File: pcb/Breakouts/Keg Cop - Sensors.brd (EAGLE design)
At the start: 17.8 x 53.8 mm, 6 parts

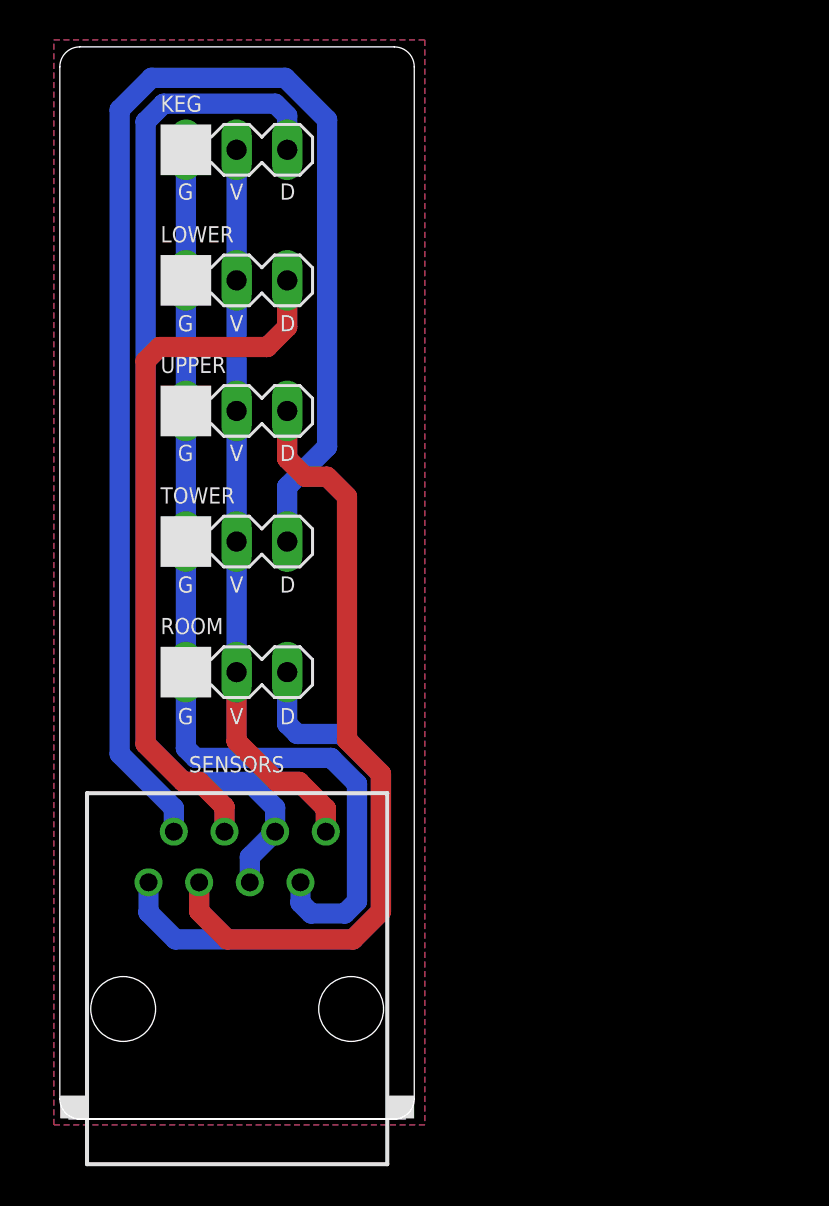
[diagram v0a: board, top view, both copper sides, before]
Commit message: Updates to names and traces
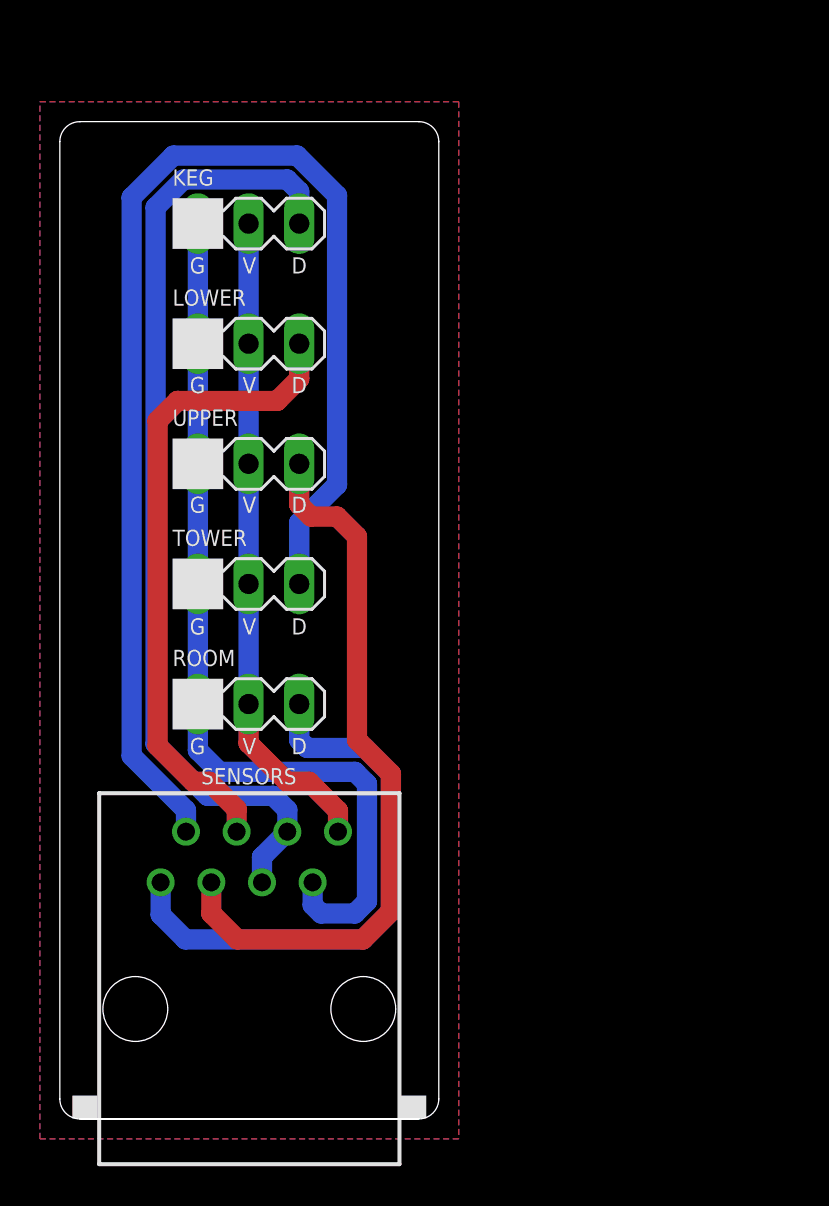
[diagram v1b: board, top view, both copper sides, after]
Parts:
- moved KEG 3.75 mm to (6.92, 44.9)
- moved LOWER 3.23 mm to (6.92, 38.9)
- moved UPPER 2.72 mm to (6.92, 32.8)
- moved TOWER 2.21 mm to (6.92, 26.8)
- moved ROOM 1.71 mm to (6.92, 20.8)
- moved SENSORS 0.61 mm to (9.50, 5.51)
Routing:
- net TDAT: track 71.2 -> 65.2 mm
- net KDAT: track 52.7 -> 48.7 mm
- net GND: track 49.6 -> 45.8 mm
- net 5V: track 36.7 -> 33.0 mm
- net LDAT: track 35.9 -> 32.4 mm
- net UDAT: track 39.4 -> 36.8 mm
- net RDAT: track 29.5 -> 28.3 mm
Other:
- board size 17.8 x 53.8 mm -> 19 x 50 mm

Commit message: New sensor board
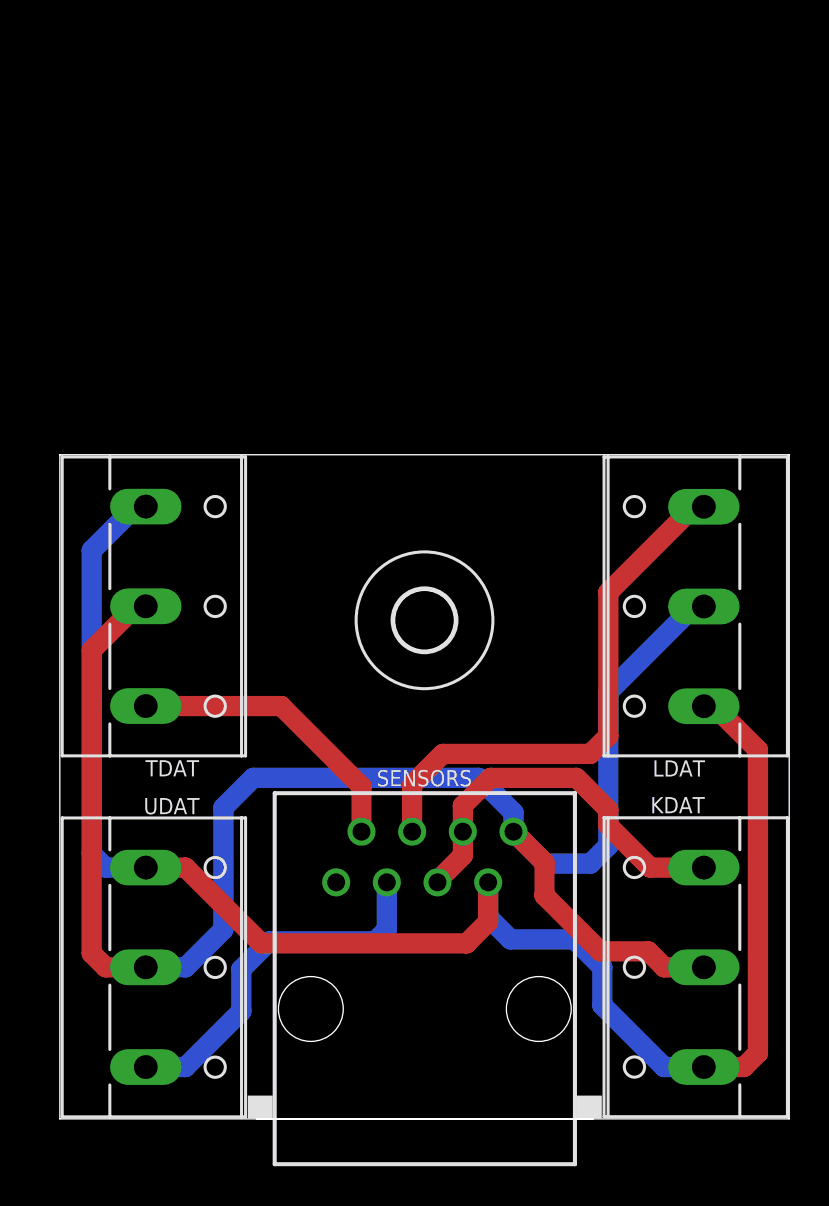
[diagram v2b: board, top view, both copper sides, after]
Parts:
- removed KEG, LOWER, ROOM, TOWER, UPPER: 3-PIN, Donnie:HDR-3_VERT
- added KDAT, LDAT, TDAT, UDAT: (no value), con-wago-500:W237-103
- added U$1: (no value), holes:3,0
- moved SENSORS 8.80 mm to (18.3, 5.51)
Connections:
- removed net RDAT: ROOM.3, SENSORS.1
- net 5V: now also KDAT.2, LDAT.2, TDAT.2, UDAT.2; no longer KEG.2, LOWER.2, ROOM.2, TOWER.2, UPPER.2
- net GND: now also KDAT.1, LDAT.1, TDAT.1, UDAT.1; no longer KEG.1, LOWER.1, ROOM.1, TOWER.1, UPPER.1
- net KDAT: now also KDAT.3; no longer KEG.3
- net LDAT: now also LDAT.3; no longer LOWER.3
- net TDAT: now also TDAT.3; no longer TOWER.3
- net UDAT: now also UDAT.3; no longer UPPER.3
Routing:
- net TDAT: track 65.2 -> 14.8 mm
- net 5V: track 33.0 -> 82.8 mm
- net GND: track 45.8 -> 81.6 mm
- net KDAT: track 48.7 -> 19.4 mm
- net RDAT: track 28.3 -> 0.00 mm
- net UDAT: track 36.8 -> 18.5 mm
- net LDAT: track 32.4 -> 27.0 mm
- removed copper zone on layer 1, net GND
- removed copper zone on layer 16, net GND
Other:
- board size 19 x 50 mm -> 36.6 x 33.3 mm
- board text removed: "D"
- board text removed: "G"
- board text removed: "V"
